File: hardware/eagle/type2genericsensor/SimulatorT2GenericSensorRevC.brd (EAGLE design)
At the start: 48.3 x 30.5 mm, 10 parts

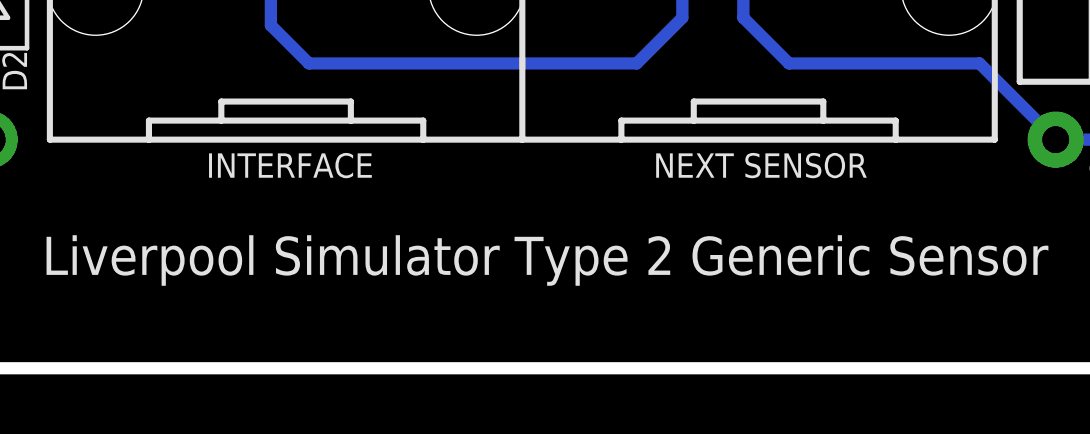
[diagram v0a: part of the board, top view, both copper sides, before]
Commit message: Board Housekeeping
URL on silkscreens, caution messages, tidy up naming conventions.
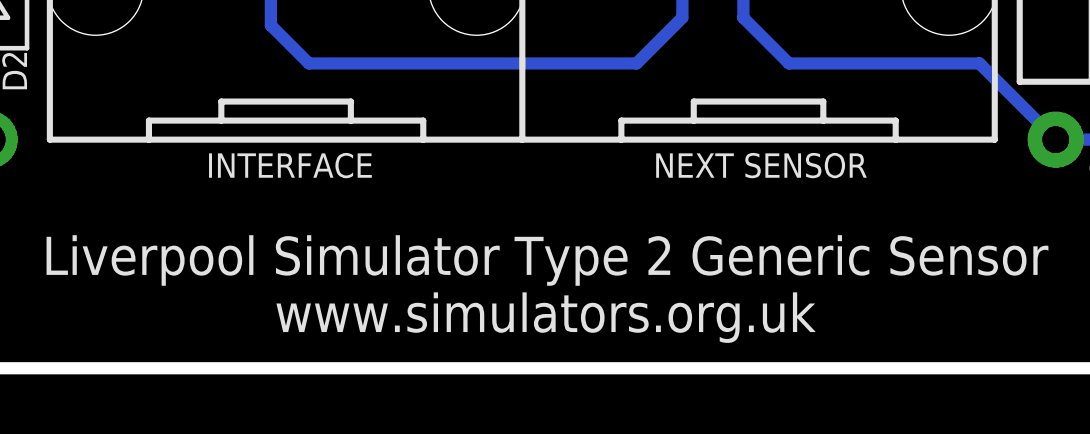
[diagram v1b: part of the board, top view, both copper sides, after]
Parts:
- added U$1: (no value), AIC_Custom:WARNING_TRIANGLE_TPLACE
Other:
- board text added: "Connect this board to Liverpool Simulator Type 2 or compatible equipment ONLY. Refer to documentation for details."
- board text added: "Liverpool Simulator Type 2 Generic Sensor www.simulators.org.uk"
- board text removed: "Liverpool Simulator Type 2 Generic Sensor"
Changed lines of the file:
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@@
 <board>
 <plain>
-<text x="24.892" y="4.3815" size="1.27" layer="21" font="vector" rot="R180" align="bottom-center">Liverpool Simulator Type 2 Generic Sensor</text>
+<text x="24.892" y="4.3815" size="1.27" layer="21" font="vector" rot="R180" align="bottom-center">Liverpool Simulator Type 2 Generic Sensor
+www.simulators.org.uk</text>
 <text x="44.069" y="25.4" size="0.762" layer="21" font="vector" rot="R180" align="center">Rev C
 01/2018</text>
@@
 <wire x1="0" y1="27.94" x2="2.54" y2="30.48" width="0.4064" layer="20" curve="-90"/>
 <text x="8.9535" y="28.321" size="0.6858" layer="21" font="vector" align="bottom-center">+   -   S</text>
+<text x="20.32" y="6.35" size="1.016" layer="22" font="vector" rot="MR0" align="center">Connect this board to
+Liverpool Simulator Type 2
+or compatible equipment ONLY.
+Refer to documentation for details.</text>
 </plain>
 <attributes>
@@
 <attribute name="VALUE" x="5.08" y="23.495" size="1.27" layer="27"/>
 </element>
+<element name="U$1" library="AIC_Custom" package="WARNING_TRIANGLE_TPLACE" value="" x="38.1" y="3.81" rot="MR0"/>
 </elements>
 <signals>
